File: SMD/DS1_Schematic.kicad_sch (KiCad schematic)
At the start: 58 parts, among them J1 AudioJack3_Switch, J2 AudioJack2_Switch, J3 BAT_CON, J4 PWR_SUPP_COM, Q1 2SC2240, Q2 2SC2240, Q3 2SC2240, U1 NE5532

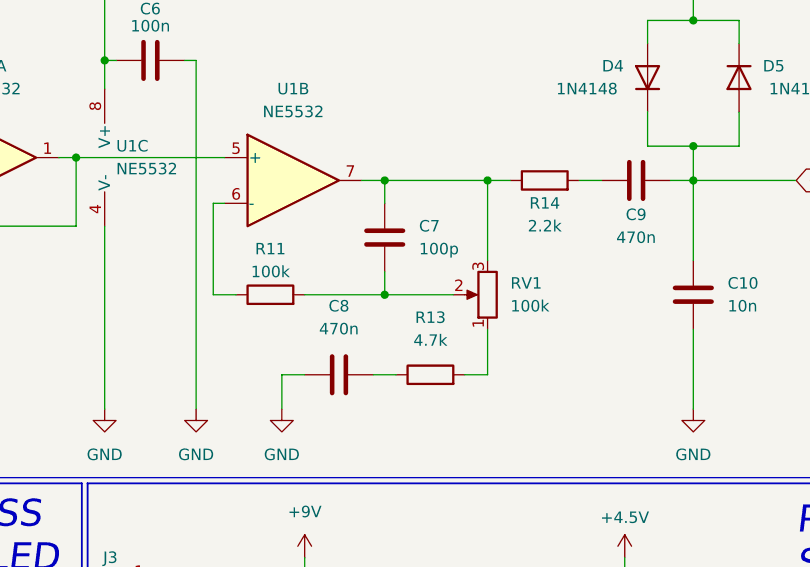
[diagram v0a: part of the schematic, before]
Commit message: new smd model
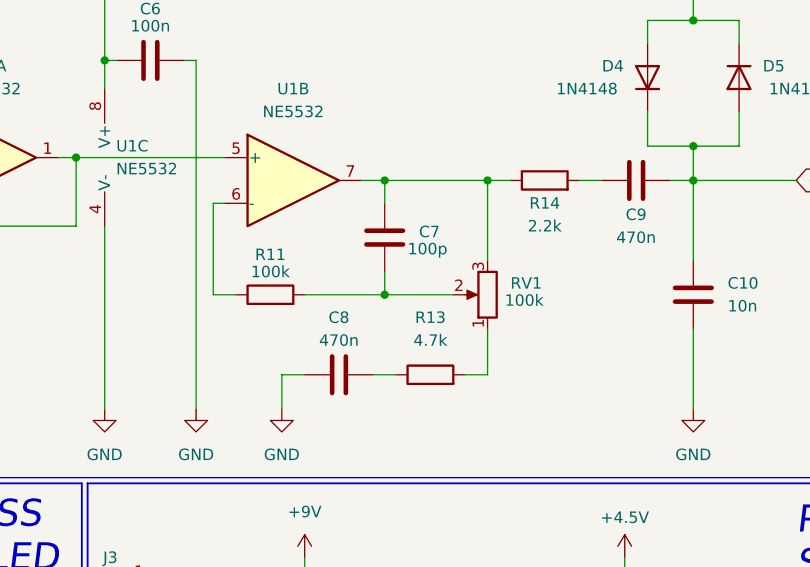
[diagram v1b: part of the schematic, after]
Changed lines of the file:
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@@
   )
   (symbol (lib_id "Device:R_Potentiometer") (at 228.6 74.295 180) (unit 1)
-    (in_bom yes) (on_board yes) (fields_autoplaced)
+    (in_bom yes) (on_board yes)
     (property "Reference" "RV1" (id 0) (at 231.14 73.0249 0)
       (effects (font (size 1.27 1.27)) (justify right))
     )
-    (property "Value" "100k" (id 1) (at 231.14 75.5649 0)
+    (property "Value" "100k" (id 1) (at 230.505 74.9299 0)
       (effects (font (size 1.27 1.27)) (justify right))
     )
@@
   (symbol (lib_id "Device:R") (at 204.47 74.295 90) (unit 1)
     (in_bom yes) (on_board yes)
-    (property "Reference" "R11" (id 0) (at 204.47 69.215 90))
+    (property "Reference" "R11" (id 0) (at 204.47 69.85 90))
     (property "Value" "100k" (id 1) (at 204.47 71.755 90))
     (property "Footprint" "Resistor_SMD:R_1206_3216Metric_Pad1.30x1.75mm_HandSolder" (id 2) (at 204.47 76.073 90)
@@
   )
   (symbol (lib_id "Device:C") (at 212.09 83.185 90) (unit 1)
-    (in_bom yes) (on_board yes) (fields_autoplaced)
-    (property "Reference" "C8" (id 0) (at 212.09 75.565 90))
-    (property "Value" "470n" (id 1) (at 212.09 78.105 90))
+    (in_bom yes) (on_board yes)
+    (property "Reference" "C8" (id 0) (at 212.09 76.835 90))
+    (property "Value" "470n" (id 1) (at 212.09 79.375 90))
     (property "Footprint" "Capacitor_SMD:C_1206_3216Metric_Pad1.33x1.80mm_HandSolder" (id 2) (at 215.9 82.2198 0)
       (effects (font (size 1.27 1.27)) hide)
@@
   )
   (symbol (lib_id "Device:C") (at 217.17 67.945 0) (unit 1)
-    (in_bom yes) (on_board yes) (fields_autoplaced)
-    (property "Reference" "C7" (id 0) (at 220.98 66.6749 0)
-      (effects (font (size 1.27 1.27)) (justify left))
-    )
-    (property "Value" "100p" (id 1) (at 220.98 69.2149 0)
-      (effects (font (size 1.27 1.27)) (justify left))
-    )
+    (in_bom yes) (on_board yes)
+    (property "Reference" "C7" (id 0) (at 220.98 67.3099 0)
+      (effects (font (size 1.27 1.27)) (justify left))
+    )
+    (property "Value" "100p" (id 1) (at 219.71 69.2149 0)
+      (effects (font (size 1.27 1.27)) (justify left))
+    )
